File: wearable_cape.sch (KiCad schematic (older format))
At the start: 33 parts, among them P1 BELA_AINS, P4 BELA_AOUTS, P5 CONN_01X04, P6 CONN_01X04, P8 BEAGLEBONEBLACK_P8, P9 BEAGLEBONEBLACK_P9, SW1 SW_PUSH, U1 MCP6004, U2 MCP6001

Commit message: schematic updates
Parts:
- removed P1: BELA_AINS, symbol BELA_AINS
- removed P8: BEAGLEBONEBLACK_P8, symbol BEAGLEBONEBLACK_P8
- removed R2: 120K, symbol R
- removed R3: 68K, symbol R
- removed U2: MCP6001, symbol MCP6001
- added C? (x2): 220pF, symbol C
- added C? (x2): 440pF, symbol C
- added C? (x2): 1uF, symbol CP1
- added P?: CONN_01X04, symbol CONN_01X04
- added P?: BATTERY_CONNECTOR, symbol BATTERY_CONNECTOR
- added P?: BEAGLEBONEBLACK_P8, symbol BEAGLEBONEBLACK_P8
- added P?: BELA_AINS, symbol BELA_AINS
- added R? (x4): 28.7k, symbol R
- added R?: 120k, symbol R
- added R?: 68k, symbol R
- added R?: 10k, symbol R
- added SW?: SW_MODE_SEL, symbol SW_PUSH
- added U2: MCP6004, symbol MCP6004
- added U?: OKI_78SR-5, symbol OKI_78SR-5
- SW1: value SW_PUSH -> SW_HALT
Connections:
- net labels added: BAT_11.1V, BELA_IN0, BELA_IN1, BELA_IN2, BELA_IN3, BELA_IN4, BELA_IN5, BELA_IN6, BELA_IN7, BELA_OUT4, BELA_OUT5, BELA_OUT6, BELA_OUT7, D0, D1, D10, D11, D12, D13, D14, D15, D2, D3, D4, D5, D6, D7, D8, D9, FILT_OUT4, FILT_OUT5, RAW_5V, REF_1.8V, SYS_3.3V, SYS_5V, ~HALT
- net labels removed: Vcc_RAW, Vref
- wire segments 98 -> 181
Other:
- moved on the sheet: C10, C11, C12, C13, C8, C9, P4, R1, R10, R11, R8, R9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

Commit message: Updates to pcb: use beagleboneblack part in schematic, update the parts that did not have proper references, import all footprints to the pcb
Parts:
- removed P9: BEAGLEBONEBLACK_P9, symbol BEAGLEBONEBLACK_P9
- removed P?: BATTERY_CONNECTOR, symbol BATTERY_CONNECTOR
- removed P?: BEAGLEBONEBLACK_P8, symbol BEAGLEBONEBLACK_P8
- removed U?: OKI_78SR-5, symbol OKI_78SR-5
- added P2: RECEIVER, Socket_Strips:Socket_Strip_Straight_2x04, symbol CONN_02X04
- added P3: BATTERY, Terminal_Blocks:TerminalBlock_Pheonix_MPT-2.54mm_2pol, symbol CONN_01X02
- added U3: BEAGLEBONEBLACK, BBB:beagleboneblack_nomount, symbol BEAGLEBONEBLACK
- added U4: OKI_7805, Socket_Strips:Socket_Strip_Angled_1x03, symbol OKI_7805
- C1, C10, C11, C2, C3, C4, C5, C8, C9: footprint (none) -> Capacitors_SMD:C_0603_HandSoldering
- C12, C13, C6, C7: footprint (none) -> SMD_Packages:SMD-1206_Pol
- C14, C15, C16, C17: renamed from C?; footprint (none) -> Capacitors_SMD:C_0603_HandSoldering
- C18, C19: renamed from C?; footprint (none) -> SMD_Packages:SMD-1206_Pol
- P1: renamed from P?; footprint (none) -> Pin_Headers:Pin_Header_Straight_1x10
- P4: footprint (none) -> Pin_Headers:Pin_Header_Straight_1x10
- P5, P6: footprint (none) -> Socket_Strips:Socket_Strip_Angled_1x04
- P7: renamed from P?; footprint (none) -> Socket_Strips:Socket_Strip_Angled_1x04
- R1, R10, R11, R4, R5, R6, R7, R8, R9: footprint (none) -> Resistors_SMD:R_0603_HandSoldering
- R12, R13, R14, R15, R16, R2, R3: renamed from R?; footprint (none) -> Resistors_SMD:R_0603_HandSoldering
- SW1: footprint (none) -> Buttons_Switches_SMD:SW_SPST_EVQPE1
- SW2: renamed from SW?; footprint (none) -> Buttons_Switches_SMD:SW_SPST_EVQPE1
- U1, U2: footprint (none) -> Housings_SOIC:SOIC-14_3.9x8.7mm_Pitch1.27mm
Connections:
- net BAT_11.1V: now also P3.2 (P2), U4.1 (VI)
- net D0: now also U3.B8 (TIMER7)
- net D1: now also U3.C8 (SYS_5V)
- net D10: now also U3.C15 (GPIO1_16)
- net D11: now also U3.C18 (I2C1_SDA)
- net D12: now also U3.B28 (GPIO2_24)
- net D13: now also U3.C28 (SPI1_CS0)
- net D14: now also U3.B30 (GPIO2_25)
- net D15: now also U3.C30 (SPI1_D1)
- net D2: now also U3.B10 (TIMER6)
- net D3: now also U3.C10 (SYS_RESETn)
- net D4: now also U3.B12 (GPIO1_12)
- net D5: now also U3.C12 (GPIO1_28)
- net D6: now also U3.C11 (UART4_RXD)
- net D7: now also U3.C13 (UART4_TXD)
- net D8: now also U3.B16 (GPIO1_14)
- net D9: now also U3.C16 (EHRPWM1B)
- net GND: now also P2.7 (P7), P3.1 (P1), U3.B1 (DGND), U3.C1 (DGND), U4.2 (GND)
- net RAW_5V: now also P2.1 (P1), U3.B5 (GPIO1_2), U3.C5 (VDD_5V), U4.3 (VO)
- net SYS_3.3V: now also U3.B3 (GPIO1_6)
- net SYS_5V: now also U3.B7 (TIMER4)
- net ~HALT: now also U3.B27 (GPIO2_22)
- new net RCV0: P2.2 (P2)
- new net RCV1: P2.4 (P4)
- new net RCV2: P2.6 (P6)
- new net RCV3: P2.8 (P8)
- new net RX: P2.3 (P3)
- new net TX: P2.5 (P5)
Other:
- moved on the sheet: C1, C10, C11, C12, C13, C14, C15, C16, C17, C18, C19, C2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

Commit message: basic routing done
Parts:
- added C20: 100nF, Capacitors_SMD:C_0603_HandSoldering, symbol C
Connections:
- net RCV0 is gone; now on net D15: P2.2 (P2)
- net RCV1 is gone; now on net D14: P2.4 (P4)
- net RCV2 is gone; now on net D13: P2.6 (P6)
- net RCV3 is gone; now on net D12: P2.8 (P8)
- net BELA_OUT0: now also R9.2; no longer R4.2
- net BELA_OUT1: now also R8.2; no longer R5.2
- net BELA_OUT2: now also R4.2; no longer R8.2
- net BELA_OUT3: now also R5.2; no longer R9.2
- net D0: now also U3.B7 (TIMER4); no longer U3.B8 (TIMER7)
- net D1: now also U3.B8 (TIMER7); no longer U3.C8 (SYS_5V)
- net D10: now also U3.C16 (EHRPWM1B); no longer U3.C15 (GPIO1_16)
- net D11: now also U3.B18 (GPIO2_1); no longer U3.C18 (I2C1_SDA)
- net D12: now also U3.B27 (GPIO2_22); no longer U3.B28 (GPIO2_24)
- net D13: now also U3.B28 (GPIO2_24); no longer U3.C28 (SPI1_CS0)
- net D14: now also U3.B29 (GPIO2_23); no longer U3.B30 (GPIO2_25)
- net D15: now also U3.B30 (GPIO2_25); no longer U3.C30 (SPI1_D1)
- net D2: now also U3.B9 (TIMER5); no longer U3.B10 (TIMER6)
- net D3: now also U3.B10 (TIMER6); no longer U3.C10 (SYS_RESETn)
- net D4: now also U3.B11 (GPIO1_13); no longer U3.B12 (GPIO1_12)
- net D5: now also U3.B12 (GPIO1_12); no longer U3.C12 (GPIO1_28)
- net D6: now also U3.C12 (GPIO1_28); no longer U3.C11 (UART4_RXD)
- net D7: now also U3.C14 (EHRPWM1A); no longer U3.C13 (UART4_TXD)
- net D8: now also U3.B15 (GPIO1_15); no longer U3.B16 (GPIO1_14)
- net D9: now also U3.B16 (GPIO1_14); no longer U3.C16 (EHRPWM1B)
- net FILT_OUT0: now also P5.2 (P2); no longer P5.1 (P1)
- net FILT_OUT1: now also P5.1 (P1); no longer P5.2 (P2)
- net GND: now also U3.B2 (DGND), U3.C2 (DGND), U3.C43 (DGND), U3.C44 (DGND), U3.C45 (DGND), U3.C46 (DGND); no longer C5.2, R3.2, U1.11 (V-), U1.11 (V-), U1.11 (V-), U1.11 (V-), U2.11 (V-), U2.11 (V-), U2.11 (V-)
- net RAW_5V: now also U3.C6 (VDD_5V); no longer U3.B5 (GPIO1_2)
- net RX: now also U3.B38 (UART5_RXD)
- net SYS_3.3V: now also U3.C4 (VDD_3V3EXP); no longer U3.B3 (GPIO1_6)
- net SYS_5V: now also U3.C7 (SYS_5V); no longer R2.1, U2.4 (V+), U3.B7 (TIMER4)
- net TX: now also U3.B37 (UART5_TXD)
- net VCC: now also P4.9 (5V), R2.1, U2.4 (V+), C20.1
- net ~HALT: now also U3.C27 (GPIO3_19); no longer U3.B27 (GPIO2_22)
- net GNDA: now reaches P4.10 (GND)
- net GNDA: now also C5.2, R3.2, U1.11 (V-), U1.11 (V-), U1.11 (V-), U1.11 (V-), U2.11 (V-), U2.11 (V-), U2.11 (V-), C20.2
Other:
- moved on the sheet: U3A, U3B, U3C, U3D

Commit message: Updates to PCB and first BOM files
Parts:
- added C21, C22: CP1, SMD_Packages:SMD-1210_Pol, symbol CP1
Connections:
- net BAT_11.1V: now also C21.1
- net GND: now also C21.2, C22.2
- net RAW_5V: now also C22.1
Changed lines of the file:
@@
 Wire Wire Line
 	10400 8050 10700 8050
-Wire Wire Line
-	10000 8550 10000 8350
 $Comp
 L OKI_7805 U4
@@
 Wire Wire Line
 	3750 2900 3525 2900
+$Comp
+L CP1 C21
+U 1 1 58088FAF
+P 9525 8275
+F 0 "C21" H 9550 8375 50  0000 L CNN
+F 1 "CP1" H 9550 8175 50  0000 L CNN
+F 2 "SMD_Packages:SMD-1210_Pol" H 9525 8275 50  0001 C CNN
+F 3 "" H 9525 8275 50  0000 C CNN
+	1    9525 8275
+	1    0    0    -1
+$EndComp
+$Comp
+L CP1 C22
+U 1 1 5808906C
+P 10550 8275
+F 0 "C22" H 10575 8375 50  0000 L CNN
+F 1 "CP1" H 10575 8175 50  0000 L CNN
+F 2 "SMD_Packages:SMD-1210_Pol" H 10550 8275 50  0001 C CNN
+F 3 "" H 10550 8275 50  0000 C CNN
+	1    10550 8275
+	1    0    0    -1
+$EndComp
+Wire Wire Line
+	9525 8050 9525 8125
+Connection ~ 9525 8050
+Wire Wire Line
+	10550 8050 10550 8125
+Connection ~ 10550 8050
+Wire Wire Line
+	9525 8425 10550 8425
+Connection ~ 10000 8425
+Wire Wire Line
+	10000 8350 10000 8550
 $EndSCHEMATC

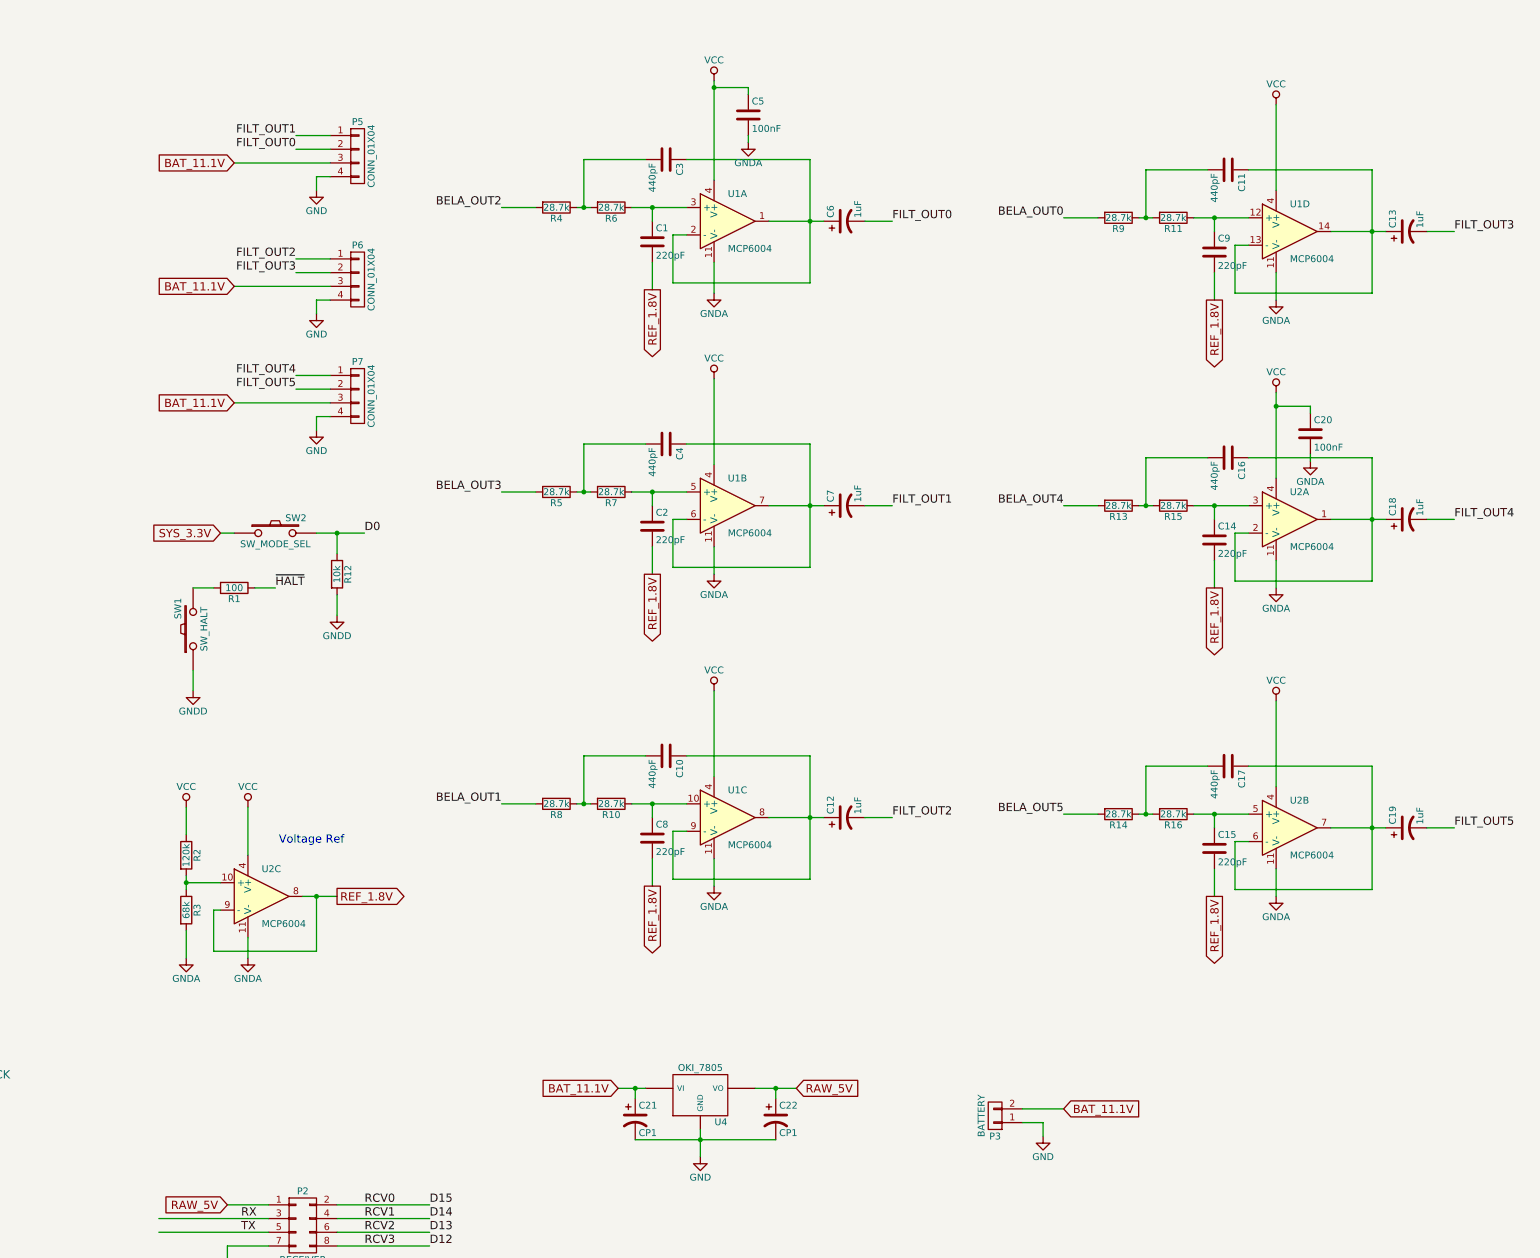
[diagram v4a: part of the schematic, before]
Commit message: updates to pcb: add attenuation, add headphone jacks, fix power supply opamps
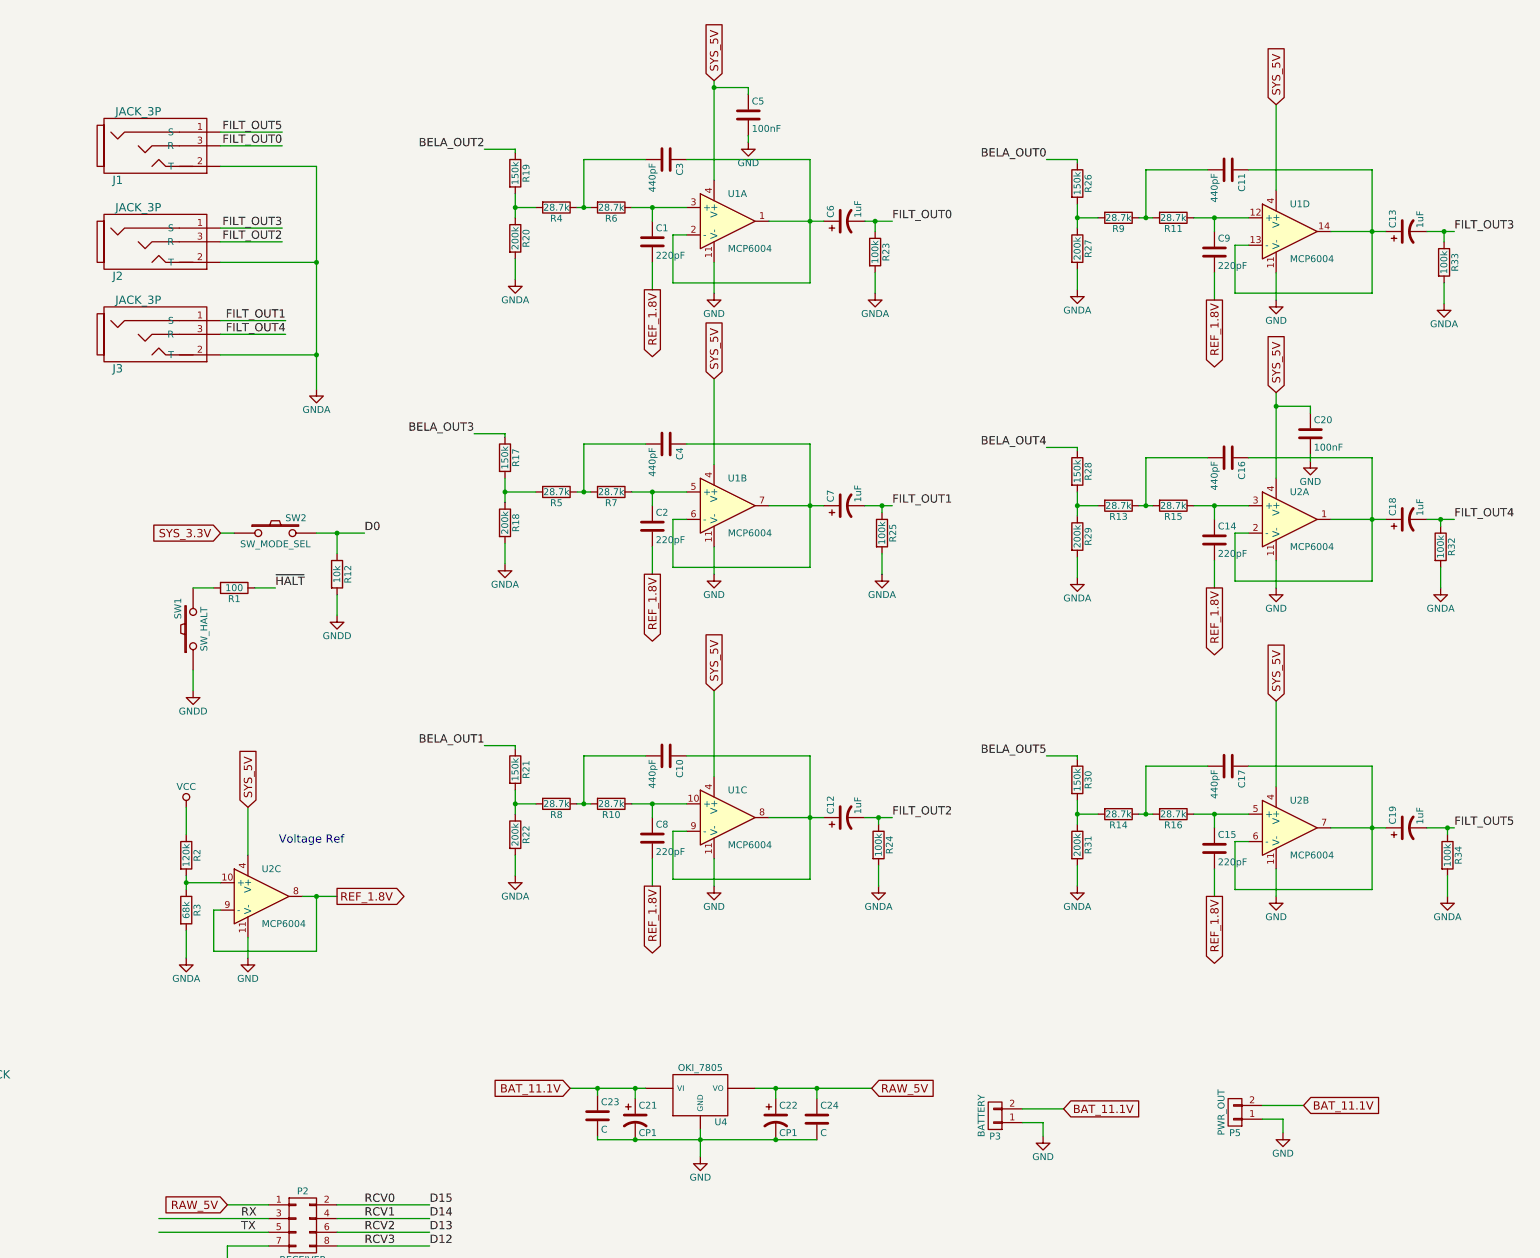
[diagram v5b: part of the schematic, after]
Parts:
- removed P5, P6, P7: CONN_01X04, Socket_Strips:Socket_Strip_Angled_1x04, symbol CONN_01X04
- added C23, C24: C, Capacitors_SMD:C_0603_HandSoldering, symbol C
- added J1, J2, J3: JACK_3P, Lumberg:Lumberg_1503_03, symbol JACK_3P
- added P5: PWR_OUT, Terminal_Blocks:TerminalBlock_Pheonix_MPT-2.54mm_2pol, symbol CONN_01X02
- added R17, R19, R21, R26, R28, R30: 150k, Resistors_SMD:R_0603_HandSoldering, symbol R
- added R18, R20, R22, R27, R29, R31: 200k, Resistors_SMD:R_0603_HandSoldering, symbol R
- added R23, R24, R25, R32, R33, R34: 100k, Resistors_SMD:R_0603_HandSoldering, symbol R
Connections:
- net BAT_11.1V: now also C23.1, P5.2 (P2)
- net BELA_OUT0: now also R26.1; no longer R9.2
- net BELA_OUT1: now also R21.1; no longer R8.2
- net BELA_OUT2: now also R19.1; no longer R4.2
- net BELA_OUT3: now also R17.1; no longer R5.2
- net BELA_OUT4: now also R28.1; no longer R13.2
- net BELA_OUT5: now also R30.1; no longer R14.2
- net FILT_OUT0: now also J1.3 (R), R23.1
- net FILT_OUT1: now also J3.1 (S), R25.1
- net FILT_OUT2: now also J2.3 (R), R24.1
- net FILT_OUT3: now also J2.1 (S), R33.1
- net FILT_OUT4: now also J3.3 (R), R32.1
- net FILT_OUT5: now also J1.1 (S), R34.1
- net GND: now also C20.2, C5.2, U1.11 (V-), U1.11 (V-), U1.11 (V-), U1.11 (V-), U2.11 (V-), U2.11 (V-), U2.11 (V-), C23.2, C24.2, P5.1 (P1)
- net GNDA: now also J1.2 (T), J2.2 (T), J3.2 (T), R18.2, R20.2, R22.2, R23.2, R24.2, R25.2, R27.2, R29.2, R31.2, R32.2, R33.2, R34.2; no longer C20.2, C5.2, U1.11 (V-), U1.11 (V-), U1.11 (V-), U1.11 (V-), U2.11 (V-), U2.11 (V-), U2.11 (V-)
- net RAW_5V: now also C24.1
- net SYS_5V: now also C20.1, C5.1, U1.4 (V+), U1.4 (V+), U1.4 (V+), U1.4 (V+), U2.4 (V+), U2.4 (V+), U2.4 (V+)
- net VCC: no longer C20.1, C5.1, U1.4 (V+), U1.4 (V+), U1.4 (V+), U1.4 (V+), U2.4 (V+), U2.4 (V+), U2.4 (V+)
- new net: R17.2, R18.1, R5.2
- new net: R19.2, R20.1, R4.2
- new net: R26.2, R27.1, R9.2
- new net: R21.2, R22.1, R8.2
- new net: R13.2, R28.2, R29.1
- new net: R14.2, R30.2, R31.1
